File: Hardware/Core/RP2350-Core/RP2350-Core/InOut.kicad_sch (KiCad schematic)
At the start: 13 parts, among them CN10 PR5L4015-5P-C-F, CN11 PR5L4015-5P-C-F, CN7 PR5L4015-5P-C-F, CN8 PR5L4015-5P-C-F, CN9 PR5L4015-5P-C-F, U35 PR5L5015-5P-C-H, U36 PR5L5015-5P-C-H, U37 PR5L5015-5P-C-H, U38 PR5L5015-5P-C-H, U39 PR5L5015-5P-C-H

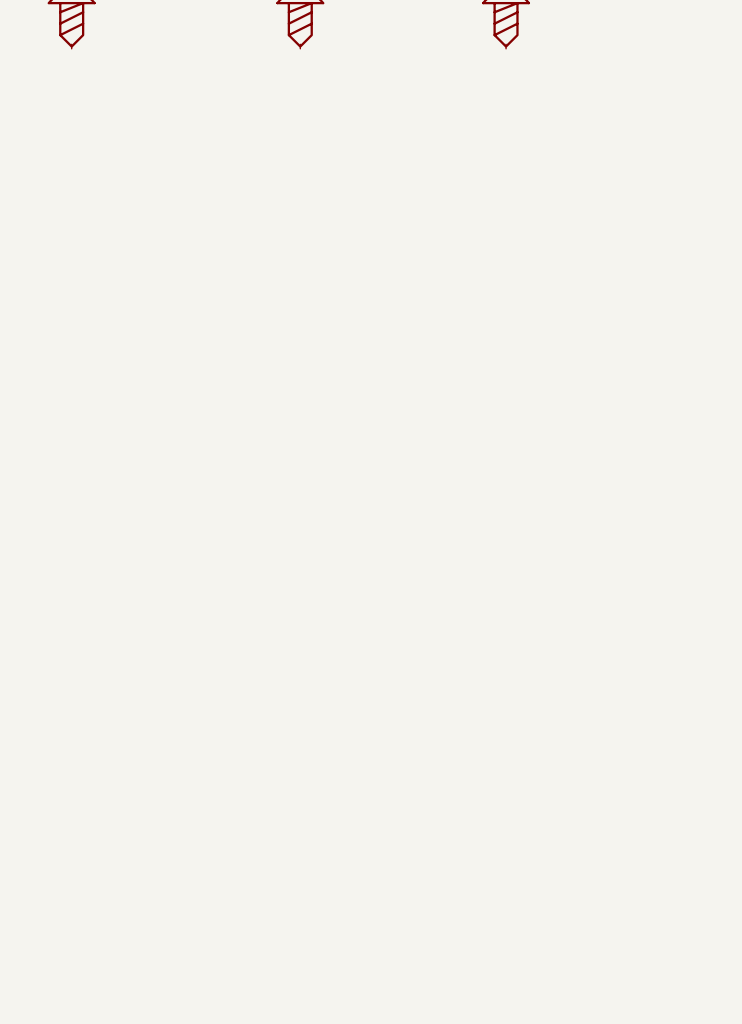
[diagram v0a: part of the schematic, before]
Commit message: Add expansion connector
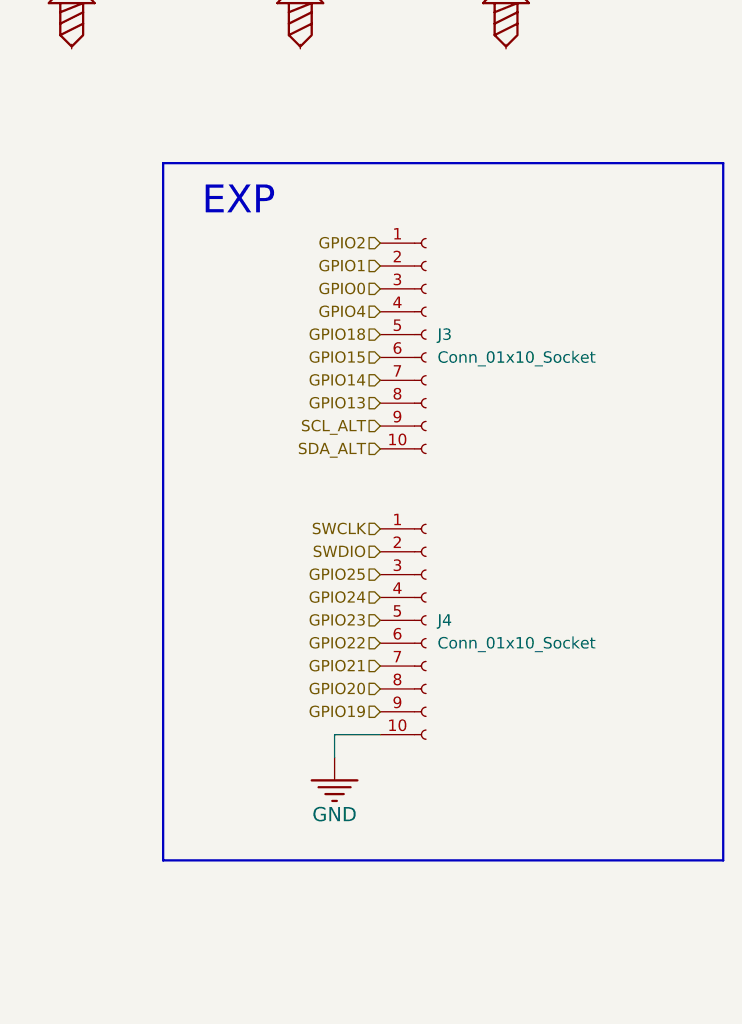
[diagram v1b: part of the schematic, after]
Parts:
- added J3, J4: Conn_01x10_Socket, symbol Connector:Conn_01x10_Socket
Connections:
- net GND: now also J4.10 (Pin_10)
- new net GPIO0: J3.3 (Pin_3)
- new net GPIO1: J3.2 (Pin_2)
- new net GPIO13: J3.8 (Pin_8)
- new net GPIO14: J3.7 (Pin_7)
- new net GPIO15: J3.6 (Pin_6)
- new net GPIO18: J3.5 (Pin_5)
- new net GPIO19: J4.9 (Pin_9)
- new net GPIO2: J3.1 (Pin_1)
- new net GPIO20: J4.8 (Pin_8)
- new net GPIO21: J4.7 (Pin_7)
- new net GPIO22: J4.6 (Pin_6)
- new net GPIO23: J4.5 (Pin_5)
- new net GPIO24: J4.4 (Pin_4)
- new net GPIO25: J4.3 (Pin_3)
- new net GPIO4: J3.4 (Pin_4)
- new net SCL_ALT: J3.9 (Pin_9)
- new net SDA_ALT: J3.10 (Pin_10)
- new net SWCLK: J4.1 (Pin_1)
- new net SWDIO: J4.2 (Pin_2)
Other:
- note added: "EXP"
